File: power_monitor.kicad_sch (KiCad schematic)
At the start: 20 parts, among them U13 ATtiny85-20S

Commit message: replace flash memory with SD flash memory; move SPI2 terminations closer to source
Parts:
- C45, C46, C47, C49, C50: Part Number CC0402KRX7R7BB104 -> CC0402KRX5R8BB104; Voltage 16 -> 25
- C48: Part Number GRM21BC81C226ME44L -> GRM21BR61E226ME44K; Voltage 16 -> 25
- R39: Part Number RC0402FR-07560RL -> RC0402JR-07560RL
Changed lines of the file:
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@@
 			)
 		)
-		(property "Datasheet" "IN-PI15TAT5R5G5B"
+		(property "Datasheet" "https://www.inolux-corp.com/datasheet/SMDLED/Addressable%20LED/IN-PI15TAT5R5G5B_v1.0.pdf"
 			(at 172.72 147.32 0)
 			(effects
@@
 			)
 		)
-		(property "Datasheet" "CDBQC0130L-HF"
+		(property "Datasheet" "https://www.comchiptech.com/admin/files/product/CDBQC0130L-HF%20RevB681116.pdf"
 			(at 154.94 85.09 0)
 			(effects
@@
 			)
 		)
-		(property "Part Number" "CC0402KRX7R7BB104"
+		(property "Part Number" "CC0402KRX5R8BB104"
 			(at 77.47 62.23 0)
 			(effects
@@
 			)
 		)
-		(property "Voltage" "16"
+		(property "Voltage" "25"
 			(at 77.47 62.23 0)
 			(effects
@@
 			)
 		)
-		(property "Part Number" "RC0402FR-07560RL"
+		(property "Part Number" "RC0402JR-07560RL"
 			(at 76.2 147.32 0)
 			(effects
@@
 			)
 		)
-		(property "Datasheet" "IN-PI15TAT5R5G5B"
+		(property "Datasheet" "https://www.inolux-corp.com/datasheet/SMDLED/Addressable%20LED/IN-PI15TAT5R5G5B_v1.0.pdf"
 			(at 80.01 147.32 0)
 			(effects
@@
 			)
 		)
-		(property "Part Number" "CC0402KRX7R7BB104"
+		(property "Part Number" "CC0402KRX5R8BB104"
 			(at 120.65 135.89 0)
 			(effects
@@
 			)
 		)
-		(property "Voltage" "16"
+		(property "Voltage" "25"
 			(at 120.65 135.89 0)
 			(effects
@@
 			)
 		)
-		(property "Part Number" "CC0402KRX7R7BB104"
+		(property "Part Number" "CC0402KRX5R8BB104"
 			(at 213.36 137.16 0)
 			(effects
@@
 			)
 		)
-		(property "Voltage" "16"
+		(property "Voltage" "25"
 			(at 213.36 137.16 0)
 			(effects
@@
 			)
 		)
-		(property "Datasheet" "IN-PI15TAT5R5G5B"
+		(property "Datasheet" "https://www.inolux-corp.com/datasheet/SMDLED/Addressable%20LED/IN-PI15TAT5R5G5B_v1.0.pdf"
 			(at 125.73 147.32 0)
 			(effects
@@
 			)
 		)
-		(property "Part Number" "GRM21BC81C226ME44L"
+		(property "Part Number" "GRM21BR61E226ME44K"
 			(at 64.77 137.16 0)
 			(effects
@@
 			)
 		)
-		(property "Voltage" "16"
+		(property "Voltage" "25"
 			(at 64.77 137.16 0)
 			(effects
@@
 			)
 		)
-		(property "Part Number" "CC0402KRX7R7BB104"
+		(property "Part Number" "CC0402KRX5R8BB104"
 			(at 166.37 135.89 0)
 			(effects
@@
 			)
 		)
-		(property "Voltage" "16"
+		(property "Voltage" "25"
 			(at 166.37 135.89 0)
 			(effects
@@
 			)
 		)
-		(property "Part Number" "CC0402KRX7R7BB104"
+		(property "Part Number" "CC0402KRX5R8BB104"
 			(at 74.93 137.16 0)
 			(effects
@@
 			)
 		)
-		(property "Voltage" "16"
+		(property "Voltage" "25"
 			(at 74.93 137.16 0)
 			(effects
@@
 			)
 		)
-		(property "Datasheet" "IN-PI15TAT5R5G5B"
+		(property "Datasheet" "https://www.inolux-corp.com/datasheet/SMDLED/Addressable%20LED/IN-PI15TAT5R5G5B_v1.0.pdf"
 			(at 218.44 147.32 0)
 			(effects

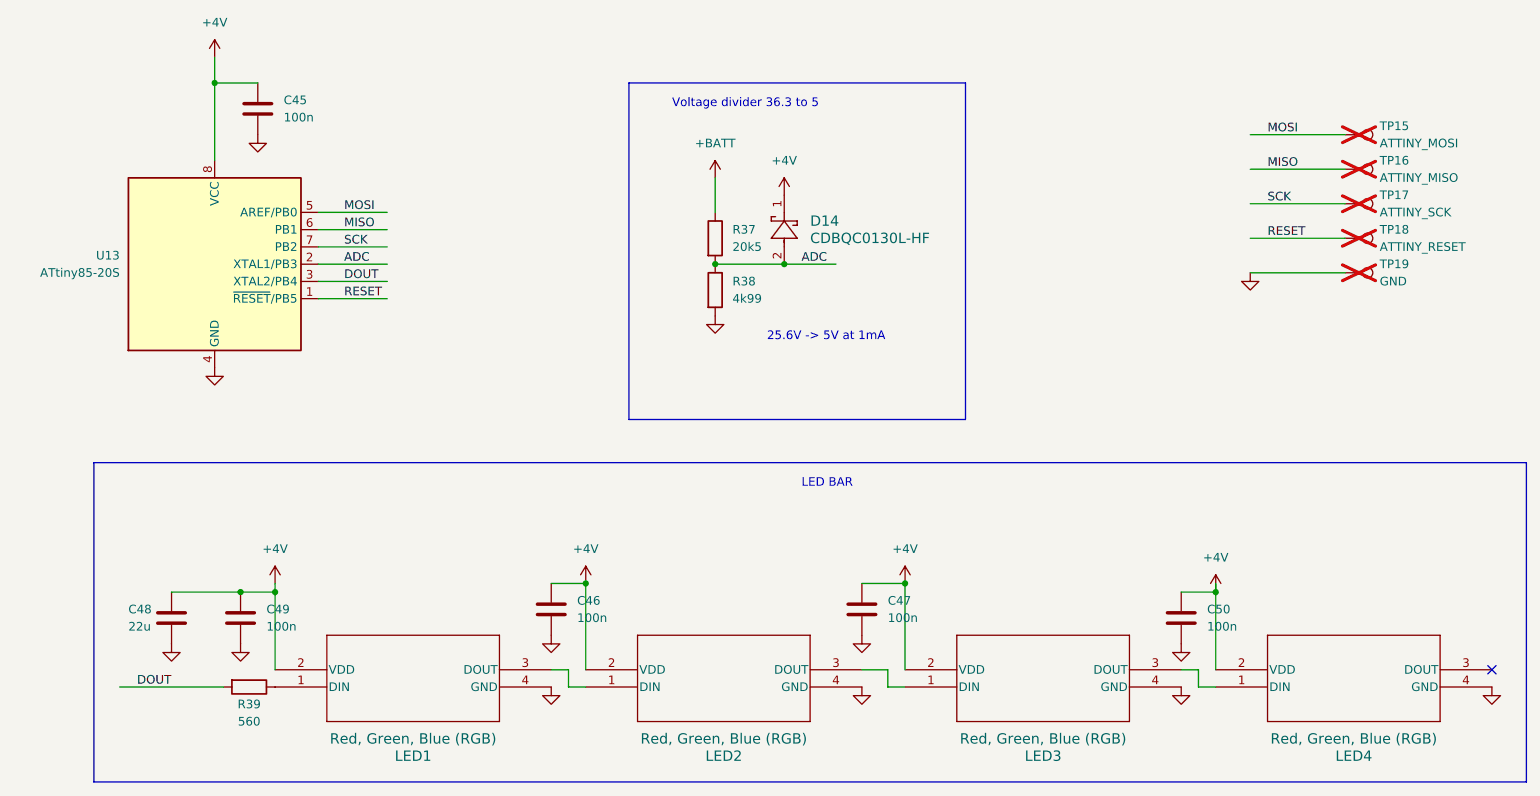
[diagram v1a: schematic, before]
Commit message: relabel components by sheet and block
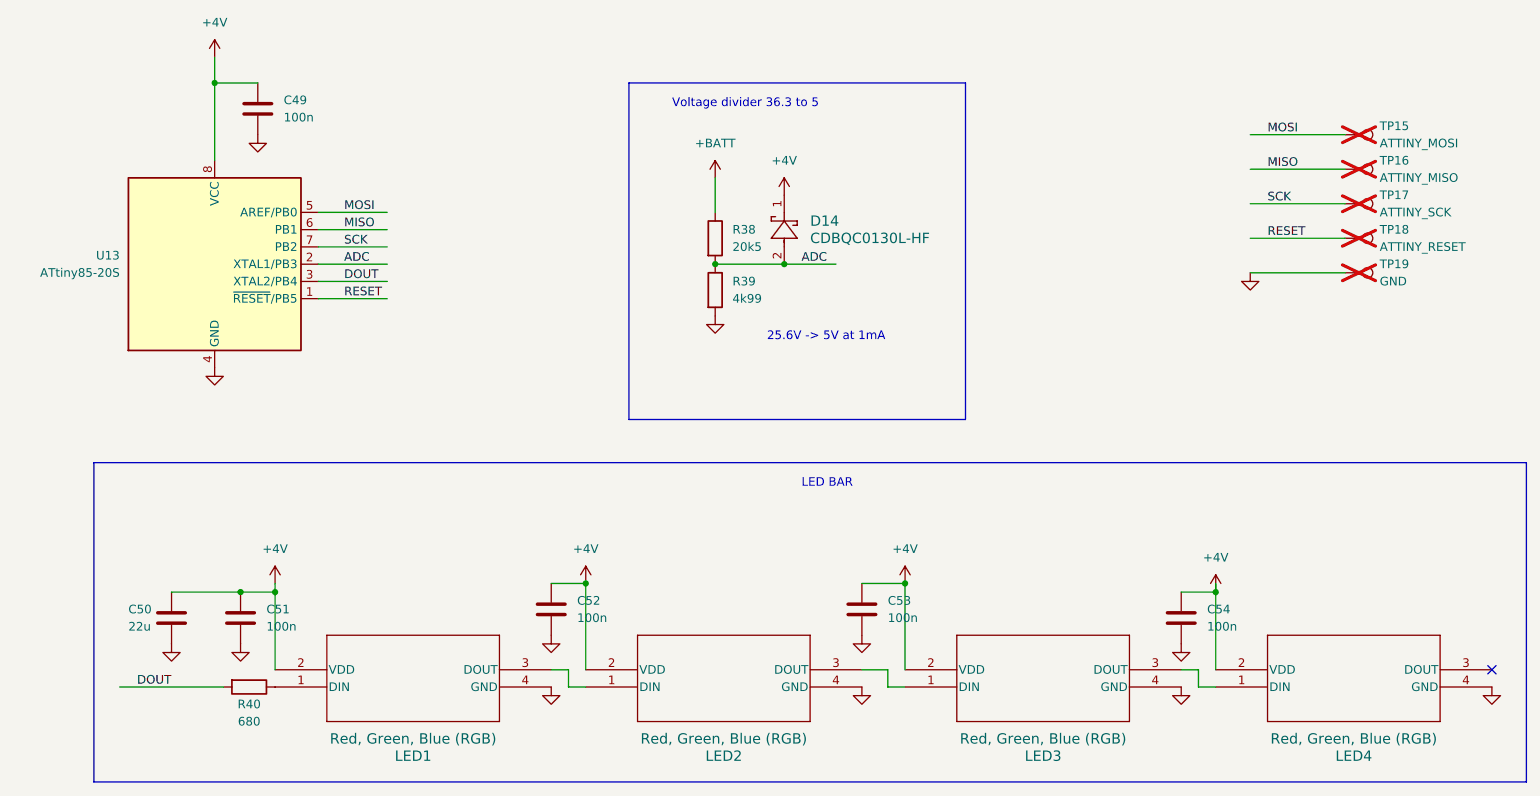
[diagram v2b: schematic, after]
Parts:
- R40: renamed from R39; value 560 -> 680; Part Number RC0402JR-07560RL -> RC0402FR-07680RP
- renumbered C45 to C49, C48 to C50, C49 to C51, C46 to C52, C47 to C53, C50 to C54, R37 to R38, R38 to R39

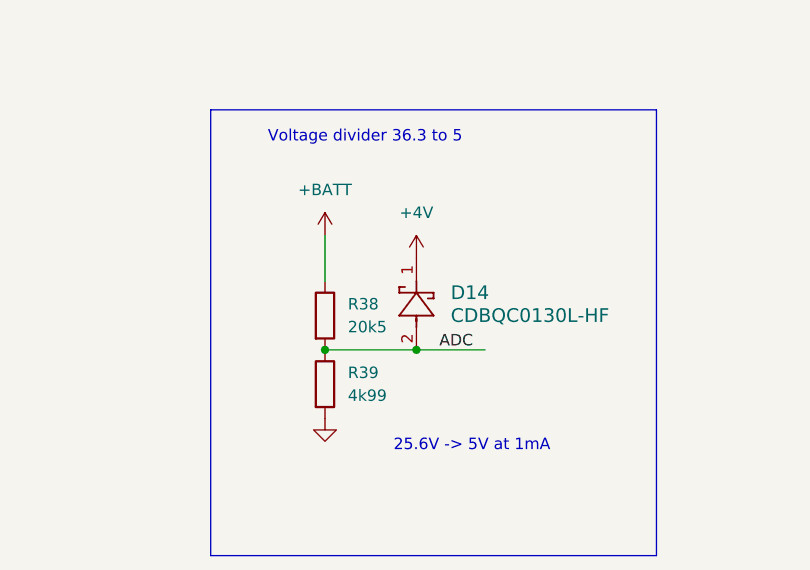
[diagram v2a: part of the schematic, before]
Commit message: remove blind vias and use 0201 resistors
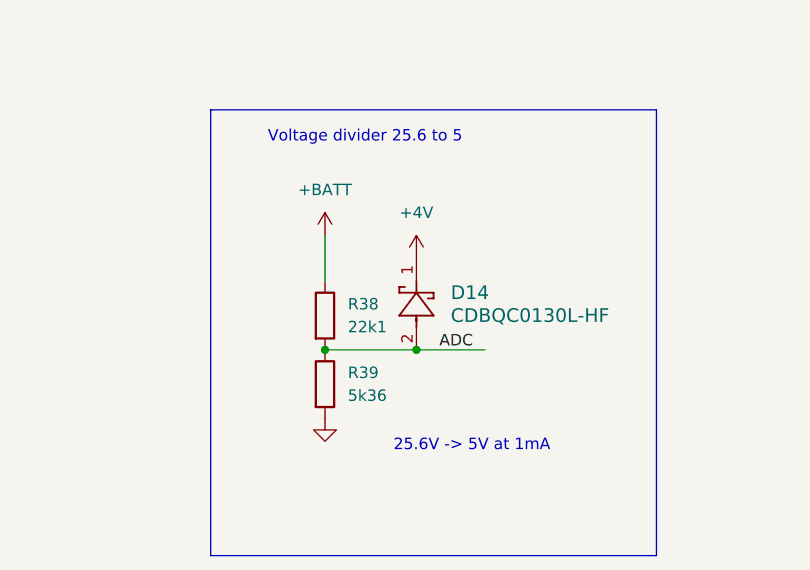
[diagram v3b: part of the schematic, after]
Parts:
- C49, C51, C52, C53, C54: footprint Capacitor_SMD:C_0402_1005Metric -> Project:C_0201_0603Metric; Manufactorer YAGEO -> Murata; Part Number CC0402KRX5R8BB104 -> GRM033R61E104KE14J
- R38: value 20k5 -> 22k1; footprint Resistor_SMD:R_0402_1005Metric -> Project:R_0201_0603Metric; Part Number RT0402BRD0720K5L -> RC0201FR-0722K1L; Tolerance 0.1% -> 1%
- R39: value 4k99 -> 5k36; footprint Resistor_SMD:R_0402_1005Metric -> Project:R_0201_0603Metric; Part Number RT0402BRD074K99L -> RC0201FR-075K36L; Tolerance 0.1% -> 1%
- R40: footprint Resistor_SMD:R_0402_1005Metric -> Project:R_0201_0603Metric; Part Number RC0402FR-07680RP -> RC0201FR-07680RL
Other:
- note added: "Voltage divider 25.6 to 5"
- note removed: "Voltage divider 36.3 to 5"
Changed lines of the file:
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@@
 		)
 	)
-	(text "Voltage divider 36.3 to 5"
+	(text "Voltage divider 25.6 to 5"
 		(exclude_from_sim no)
 		(at 138.43 62.23 0)
@@
 		(fields_autoplaced yes)
 		(property "Reference" "R39"
-			(at 147.32 87.63 0)
+			(at 147.32 87.6299 0)
 			(effects
 				(font
@@
 			)
 		)
-		(property "Value" "4k99"
-			(at 147.32 90.17 0)
+		(property "Value" "5k36"
+			(at 147.32 90.1699 0)
 			(effects
 				(font
@@
 			)
 		)
-		(property "Footprint" "Resistor_SMD:R_0402_1005Metric"
+		(property "Footprint" "Project:R_0201_0603Metric"
 			(at 143.002 88.9 90)
 			(effects
@@
 			)
 		)
-		(property "Tolerance" "0.1%"
+		(property "Tolerance" "1%"
 			(at 144.78 88.9 0)
 			(effects
@@
 			)
 		)
-		(property "Part Number" "RT0402BRD074K99L"
+		(property "Part Number" "RC0201FR-075K36L"
 			(at 144.78 88.9 0)
 			(effects
@@
 			)
 		)
-		(property "Footprint" "Capacitor_SMD:C_0402_1005Metric"
+		(property "Footprint" "Project:C_0201_0603Metric"
 			(at 78.4352 66.04 0)
 			(effects
@@
 			)
 		)
-		(property "Manufactorer" "YAGEO"
+		(property "Manufactorer" "Murata"
 			(at 77.47 62.23 0)
 			(effects
@@
 			)
 		)
-		(property "Part Number" "CC0402KRX5R8BB104"
+		(property "Part Number" "GRM033R61E104KE14J"
 			(at 77.47 62.23 0)
 			(effects
@@
 			)
 		)
-		(property "Footprint" "Resistor_SMD:R_0402_1005Metric"
+		(property "Footprint" "Project:R_0201_0603Metric"
 			(at 76.2 145.542 90)
 			(effects
@@
 			)
 		)
-		(property "Part Number" "RC0402FR-07680RP"
+		(property "Part Number" "RC0201FR-07680RL"
 			(at 76.2 147.32 0)
 			(effects
@@
 			)
 		)
-		(property "Footprint" "Capacitor_SMD:C_0402_1005Metric"
+		(property "Footprint" "Project:C_0201_0603Metric"
 			(at 121.6152 139.7 0)
 			(effects
@@
 			)
 		)
-		(property "Manufactorer" "YAGEO"
+		(property "Manufactorer" "Murata"
 			(at 120.65 135.89 0)
 			(effects
@@
 			)
 		)
-		(property "Part Number" "CC0402KRX5R8BB104"
+		(property "Part Number" "GRM033R61E104KE14J"
 			(at 120.65 135.89 0)
 			(effects
@@
 			)
 		)
-		(property "Footprint" "Capacitor_SMD:C_0402_1005Metric"
+		(property "Footprint" "Project:C_0201_0603Metric"
 			(at 214.3252 140.97 0)
 			(effects
@@
 			)
 		)
-		(property "Manufactorer" "YAGEO"
+		(property "Manufactorer" "Murata"
 			(at 213.36 137.16 0)
 			(effects
@@
 			)
 		)
-		(property "Part Number" "CC0402KRX5R8BB104"
+		(property "Part Number" "GRM033R61E104KE14J"
 			(at 213.36 137.16 0)
 			(effects
@@
 			)
 		)
-		(property "Footprint" "Capacitor_SMD:C_0402_1005Metric"
+		(property "Footprint" "Project:C_0201_0603Metric"
 			(at 167.3352 139.7 0)
 			(effects
@@
 			)
 		)
-		(property "Manufactorer" "YAGEO"
+		(property "Manufactorer" "Murata"
 			(at 166.37 135.89 0)
 			(effects
@@
 			)
 		)
-		(property "Part Number" "CC0402KRX5R8BB104"
+		(property "Part Number" "GRM033R61E104KE14J"
 			(at 166.37 135.89 0)
 			(effects
@@
 			)
 		)
-		(property "Footprint" "Capacitor_SMD:C_0402_1005Metric"
+		(property "Footprint" "Project:C_0201_0603Metric"
 			(at 75.8952 140.97 0)
 			(effects
@@
 			)
 		)
-		(property "Manufactorer" "YAGEO"
+		(property "Manufactorer" "Murata"
 			(at 74.93 137.16 0)
 			(effects
@@
 			)
 		)
-		(property "Part Number" "CC0402KRX5R8BB104"
+		(property "Part Number" "GRM033R61E104KE14J"
 			(at 74.93 137.16 0)
 			(effects
@@
 		(fields_autoplaced yes)
 		(property "Reference" "R38"
-			(at 147.32 80.01 0)
+			(at 147.32 80.0099 0)
 			(effects
 				(font
@@
 			)
 		)
-		(property "Value" "20k5"
-			(at 147.32 82.55 0)
+		(property "Value" "22k1"
+			(at 147.32 82.5499 0)
 			(effects
 				(font
@@
 			)
 		)
-		(property "Footprint" "Resistor_SMD:R_0402_1005Metric"
+		(property "Footprint" "Project:R_0201_0603Metric"
 			(at 143.002 81.28 90)
 			(effects
@@
 			)
 		)
-		(property "Tolerance" "0.1%"
+		(property "Tolerance" "1%"
 			(at 144.78 81.28 0)
 			(effects
@@
 			)
 		)
-		(property "Part Number" "RT0402BRD0720K5L"
+		(property "Part Number" "RC0201FR-0722K1L"
 			(at 144.78 81.28 0)
 			(effects
